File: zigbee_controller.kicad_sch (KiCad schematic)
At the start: 65 parts, among them J1 +24V, J10 IO23 load, J11 IO20 load, J12 IO22 load, J13 IO21 load, J2 5v, J3 Conn_01x06, J4 Conn_01x07, J5 Conn_01x05, P1 USB_C_Receptacle_GCT_USB4105, Q2 IRLB3813, Q3 IRLB3813, Q4 IRLB3813, Q5 IRLB3813, SW2 EN, SW4 Boot, U1 TPS54560, U2 ESP32-C6-MINI-1, U3 AMS1117-3.3, U4 TC4427, U5 TC4427

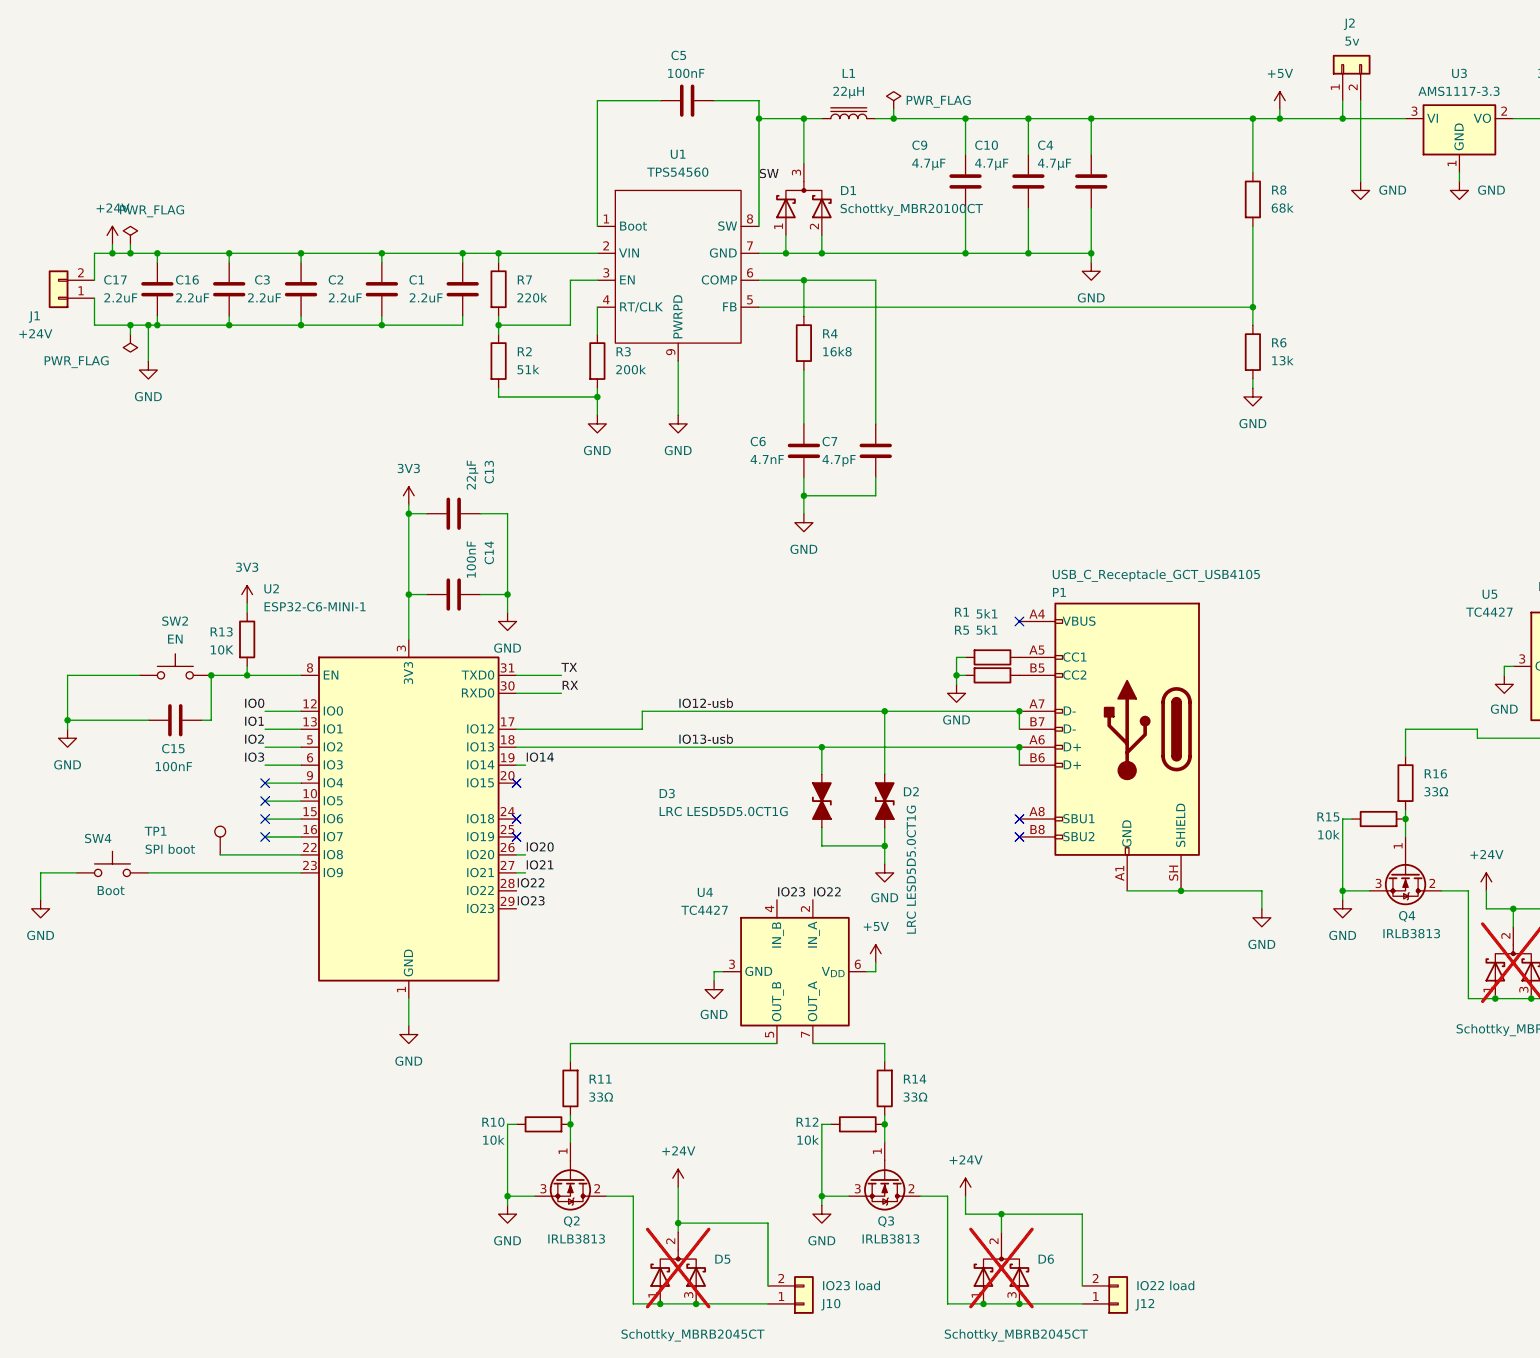
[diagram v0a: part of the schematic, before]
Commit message: 5 channels, well described BOM consolidated
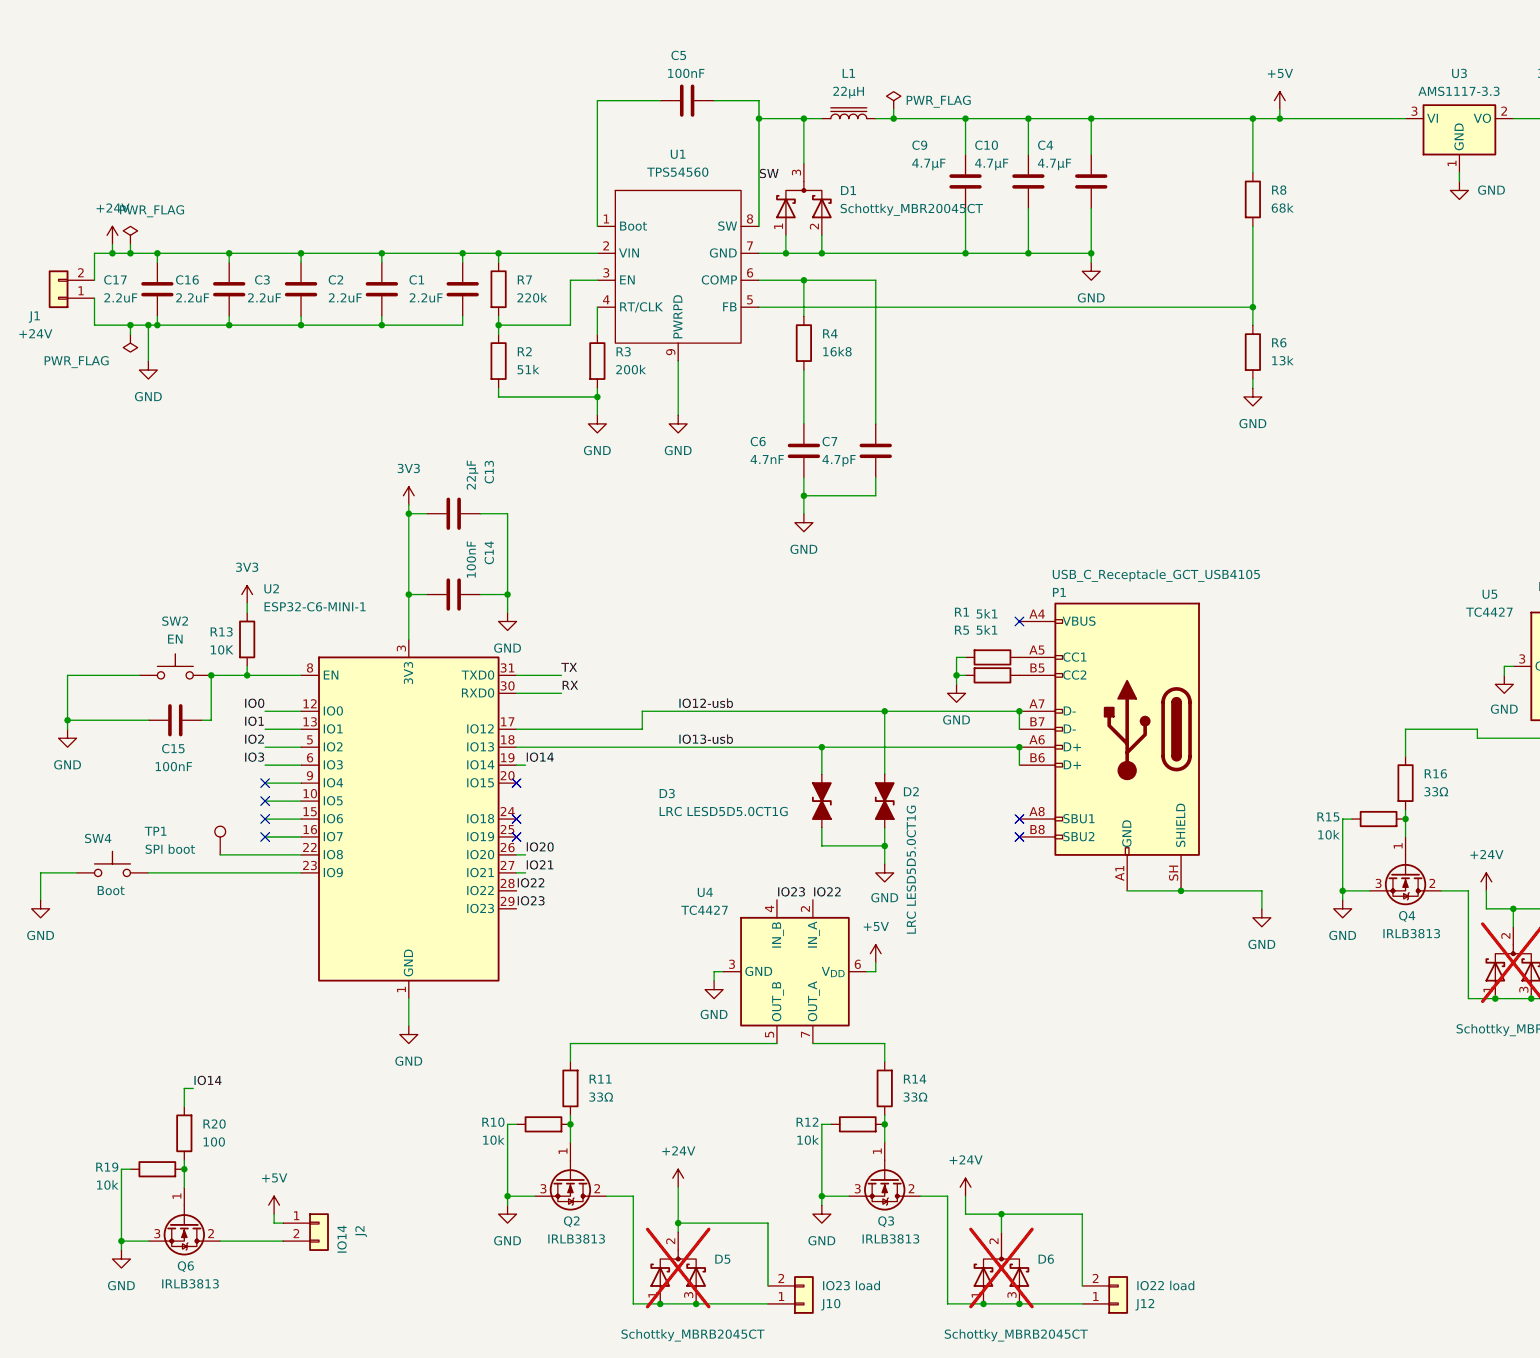
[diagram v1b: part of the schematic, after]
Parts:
- added Q6: IRLB3813, Package_TO_SOT_THT:TO-220-3_Vertical, symbol Transistor_FET:IRLB8721PBF
- added R19: 10k, Resistor_SMD:R_1206_3216Metric_Pad1.30x1.75mm_HandSolder, symbol Device:R
- added R20: 100, Resistor_SMD:R_1206_3216Metric_Pad1.30x1.75mm_HandSolder, symbol Device:R
- D1: value Schottky_MBR20100CT -> Schottky_MBR20045CT
- J2: value 5v -> IO14
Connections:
- net GND: now also Q6.3 (S), R19.1; no longer J2.2 (Pin_2)
- net IO14: now also R20.2
- new net: J2.2 (Pin_2), Q6.2 (D)
- new net: Q6.1 (G), R19.2, R20.1

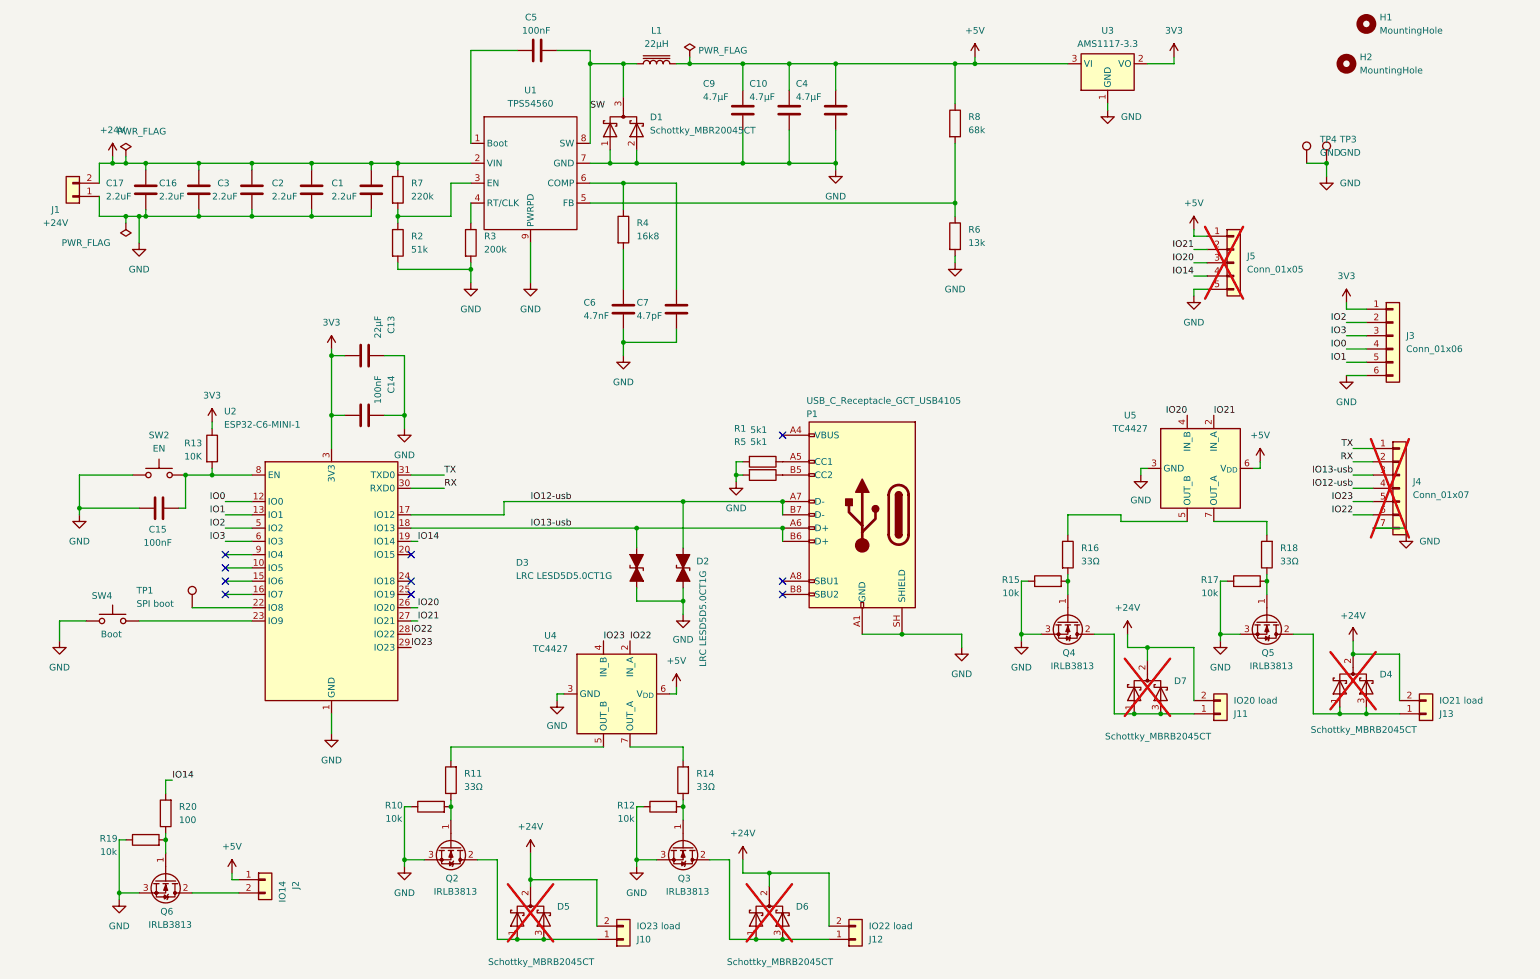
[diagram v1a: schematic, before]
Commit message: 5 channels, well described BOM consolidated
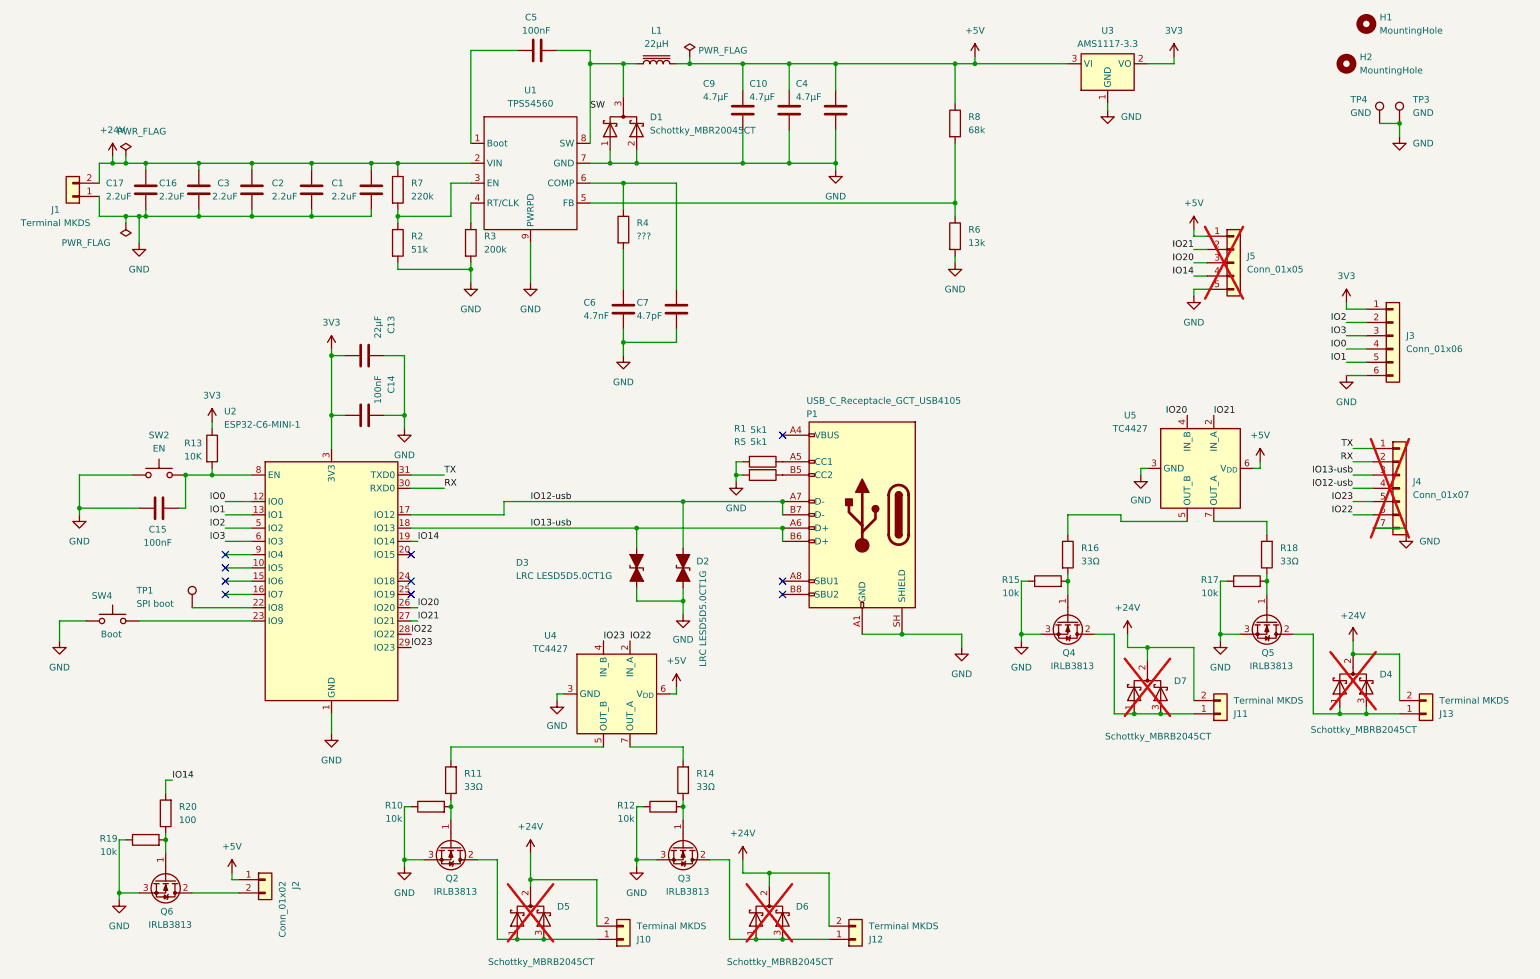
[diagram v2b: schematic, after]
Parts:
- C1, C10, C13, C14, C16, C17, C2, C3, C4, C5, C9, J5, R16, R2, R3, R6, R7, R8, U1: in_stock (none) -> yes
- C15, R11, R14, R18, R20: in_stock ordered -> yes
- D1: in_stock (none) -> 5 (20100)
- D2, D3, D4, D5, D6, D7, L1, P1, U2, U4, U5: in_stock (none) -> no
- H1, H2, J4, TP1: in_stock (none) -> -
- J1: value +24V -> Terminal MKDS; in_stock (none) -> no
- J10: value IO23 load -> Terminal MKDS; in_stock (none) -> no
- J11: value IO20 load -> Terminal MKDS; in_stock (none) -> no
- J12: value IO22 load -> Terminal MKDS; in_stock (none) -> no
- J13: value IO21 load -> Terminal MKDS; in_stock (none) -> no
- J2: value IO14 -> Conn_01x02; in_stock (none) -> yes
- Q2, Q3, Q4, Q5, Q6, SW2: in_stock yes -> no
- R1, R5: footprint (none) -> Resistor_SMD:R_1206_3216Metric_Pad1.30x1.75mm_HandSolder; in_stock (none) -> no
- R4: value 16k8 -> ???
- SW4: ali https://pt.aliexpress.com/item/1005010413616439.html?spm=a2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 -> (none); in_stock yes -> no
- TP3, TP4: in_stock (none) -> -; now left out of the parts list
- U3: in_stock (none) -> 7
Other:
- moved on the sheet: TP3, TP4

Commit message: USB power, all checks pass on PCB
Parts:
- removed R1, R5: 5k1, Resistor_SMD:R_1206_3216Metric_Pad1.30x1.75mm_HandSolder, symbol Device:R
- removed U3: AMS1117-3.3, Package_TO_SOT_SMD:SOT-223-3_TabPin2, symbol Regulator_Linear:AMS1117-3.3
- added C22: 1uF, Capacitor_SMD:C_1206_3216Metric_Pad1.33x1.80mm_HandSolder, symbol Device:C
- added C8: 1uF, Capacitor_SMD:C_1206_3216Metric, symbol Device:C
- added D8, D9: SS14, Diode_SMD:D_SMA, symbol Diode:SS14
- added JP1: CFG3-L, Jumper:SolderJumper-2_P1.3mm_Open_RoundedPad1.0x1.5mm, symbol Jumper:SolderJumper_2_Open
- added JP10, JP7, JP9: power_via_usb, Jumper:SolderJumper-2_P1.3mm_Open_RoundedPad1.0x1.5mm, symbol Jumper:SolderJumper_2_Open
- added JP2: CFG2-L, Jumper:SolderJumper-2_P1.3mm_Open_RoundedPad1.0x1.5mm, symbol Jumper:SolderJumper_2_Open
- added JP3: CFG1-L, Jumper:SolderJumper-2_P1.3mm_Open_RoundedPad1.0x1.5mm, symbol Jumper:SolderJumper_2_Open
- added JP4: CFG3-H, Jumper:SolderJumper-2_P1.3mm_Open_RoundedPad1.0x1.5mm, symbol Jumper:SolderJumper_2_Open
- added JP5: CFG2-H, Jumper:SolderJumper-2_P1.3mm_Open_RoundedPad1.0x1.5mm, symbol Jumper:SolderJumper_2_Open
- added JP6: power_via_terminal(CFG1-H), Jumper:SolderJumper-2_P1.3mm_Open_RoundedPad1.0x1.5mm, symbol Jumper:SolderJumper_2_Open
- added JP8: power_via_terminal, Jumper:SolderJumper-2_P1.3mm_Open_RoundedPad1.0x1.5mm, symbol Jumper:SolderJumper_2_Open
- added R21: 1K, Resistor_SMD:R_1206_3216Metric_Pad1.30x1.75mm_HandSolder, symbol Device:R
- added R9: 10K, Resistor_SMD:R_1206_3216Metric_Pad1.30x1.75mm_HandSolder, symbol Device:R
- added U6: RT9080, Package_TO_SOT_SMD:TSOT-23-5_HandSoldering, symbol davouds_symbol_library:RT9080
- added U9: CH224K, Package_SO:SSOP-10-1EP_3.9x4.9mm_P1mm_EP2.1x3.3mm_ThermalVias, symbol Interface_USB:CH224K
- C5, C6, C7: footprint Capacitor_SMD:C_1206_3216Metric_Pad1.33x1.80mm_HandSolder -> Capacitor_SMD:C_1206_3216Metric
- R2, R3, R4, R6, R7: footprint Resistor_SMD:R_1206_3216Metric_Pad1.30x1.75mm_HandSolder -> Resistor_SMD:R_1206_3216Metric
- TP4: value GND -> VBUS; footprint TestPoint:TestPoint_THTPad_D2.0mm_Drill1.0mm -> TestPoint:TestPoint_Pad_D2.0mm
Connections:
- net +24V: now also JP10.1 (A), JP7.1 (A), JP9.1 (A)
- net +5V: now also D9.2 (A), R21.1
- net 3V3: now also U6.5 (Vout)
- net GND: now also C22.2, C8.2, JP1.2 (B), JP2.2 (B), JP3.2 (B), U6.2 (GND), U9.11 (GND); no longer TP4.1
- net VBUS: now reaches P1.A4 (VBUS), P1.A9 (VBUS), P1.B4 (VBUS), P1.B9 (VBUS)
- net VBUS: now also TP4.1, D8.2 (A), JP10.2 (B), JP7.2 (B), JP9.2 (B), R9.2
- net CC1: now reaches P1.A5 (CC1)
- net CC1: now also U9.7 (CC1)
- net CC2: now reaches P1.B5 (CC2)
- net CC2: now also U9.6 (CC2)
- new net: JP3.1 (A), JP6.1 (A), U9.9 (CFG1)
- new net: JP2.1 (A), JP5.1 (A), U9.2 (CFG2)
- new net: JP1.1 (A), JP4.1 (A), U9.3 (CFG3)
- new net: R9.1, U9.8 (VBUS)
- new net: D8.1 (K), JP8.1 (A)
- new net CH224k_Vdd: C22.1, JP4.2 (B), JP5.2 (B), JP6.2 (B), R21.2, U9.1 (VDD)
- new net USB_5V: C8.1, D9.1 (K), JP8.2 (B), U6.1 (Vin), U6.3 (EN)
- no-connect marks 10 -> 12
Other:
- moved on the sheet: C1, C10, C13, C14, C15, C16, C17, C2, C3, C4, C5, C6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
